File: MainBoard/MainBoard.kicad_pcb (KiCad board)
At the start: 4 copper layers, 60.5 x 128.5 mm, 46 parts, among them J2 TSW-116-12-T-S, U1 TL074CN

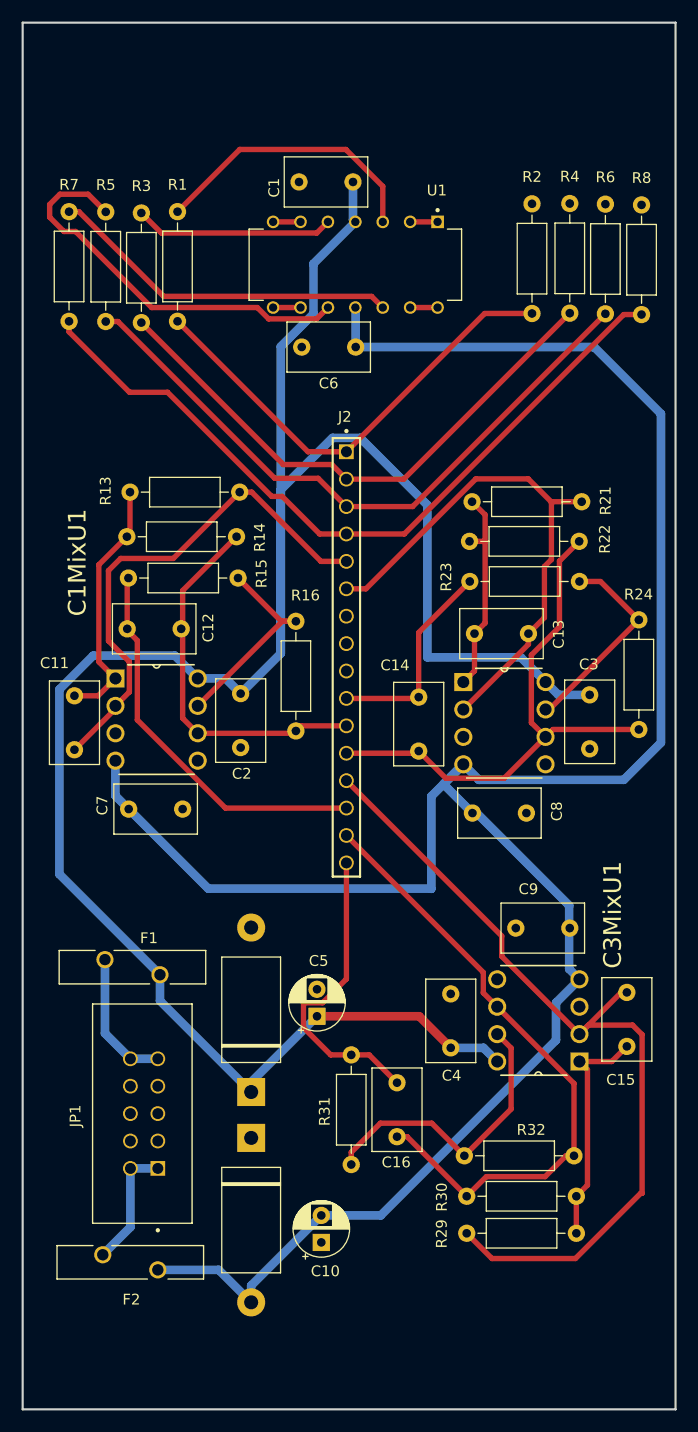
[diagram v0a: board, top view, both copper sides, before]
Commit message: added footprints and 3dmodels
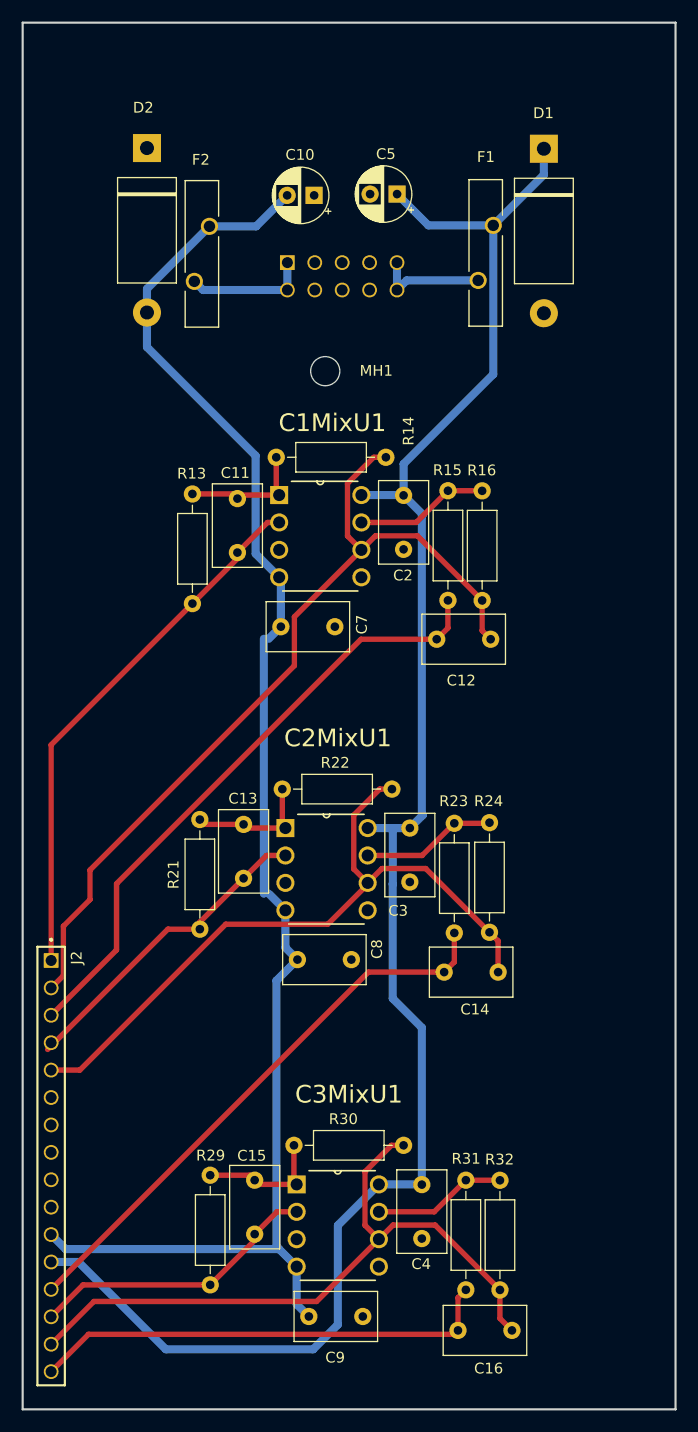
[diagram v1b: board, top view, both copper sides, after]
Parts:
- removed C1, C6: 0.1uf, Capacitor_THT:C_Disc_D7.5mm_W4.4mm_P5.00mm
- removed R1, R3, R5, R7: 1k, Resistor_THT:R_Axial_DIN0207_L6.3mm_D2.5mm_P10.16mm_Horizontal
- removed R2, R4, R6, R8: 100k, Resistor_THT:R_Axial_DIN0207_L6.3mm_D2.5mm_P10.16mm_Horizontal
- removed U1: TL074CN, TL074CN:DIP794W45P254L1969H508Q14
- added MH1: MountingHole_2.7mm_M2.5, MountingHole:MountingHole_2.7mm_M2.5, F.Cu at (129.5, 64.8)
- JP1: moved to B.Cu
- moved C10 97.0 mm to (128.5, 48.5), turned to 180 degrees
- moved F2 93.7 mm to (118.1, 53.9), turned to -90 degrees
- moved D2 92.2 mm to (113.0, 51.7)
- moved JP1 84.8 mm to (126.0, 54.7), turned to 0 degrees
- moved D1 77.1 mm to (149.8, 51.8), turned to -90 degrees
- moved C5 76.6 mm to (136.2, 48.4), turned to 180 degrees
- moved F1 73.8 mm to (144.4, 53.8), turned to -90 degrees
- moved J2 54.5 mm to (104.1, 119.4)
- moved R21 53.1 mm to (117.9, 116.5), turned to 90 degrees
- moved C9 43.4 mm to (128.0, 152.4), turned to 0 degrees
- moved C15 36.7 mm to (123.0, 139.7), turned to -90 degrees
- moved C3MixU1 28.8 mm to (134.5, 147.8), turned to 0 degrees
- moved R22 28.8 mm to (135.7, 103.5)
- moved C12 28.7 mm to (139.9, 89.6)
- moved C13 27.8 mm to (122.0, 106.8), turned to -90 degrees
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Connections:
- J2 pad 01: Input1 -> C1MixLadderOut
- J2 pad 02: Input2 -> C1MixModeOut
- J2 pad 03: Input3 -> C1MixOut
- J2 pad 04: Input4 -> C2MixLadderOut
- J2 pad 05: C1MixLadderOut -> C2MixModeOut
- J2 pad 06: C2MixLadderOut -> GND
- J2 pad 10: C2MixOut -> GND
- J2 pad 11: C1MixModeOut -> -v
- J2 pad 12: C2MixModeOut -> +v
- J2 pad 13: C3MixLadderOut -> C2MixOut
- J2 pad 14: C1MixOut -> C3MixLadderOut
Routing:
- net -v: track 216.0 -> 142.2 mm
- net Input4: track 70.2 -> 0.00 mm
- net Input3: track 60.8 -> 0.00 mm
- net Input2: track 52.1 -> 0.00 mm
- net C3MixLadderOut: track 79.1 -> 27.1 mm
- net C1MixModeOut: track 34.9 -> 81.9 mm
- net Input1: track 43.2 -> 0.00 mm
- net Net-(U1-3IN+): track 37.6 -> 0.00 mm
- net +v: track 208.0 -> 172.8 mm
- net C2MixOut: track 19.4 -> 52.6 mm
- net Net-(U1-4IN+): track 32.8 -> 0.00 mm
- net Net-(U1-1IN+): track 26.1 -> 0.00 mm
- net C1MixOut: track 36.3 -> 57.8 mm
- net C2MixLadderOut: track 49.6 -> 29.9 mm
- net Net-(U1-2IN+): track 18.5 -> 0.00 mm
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
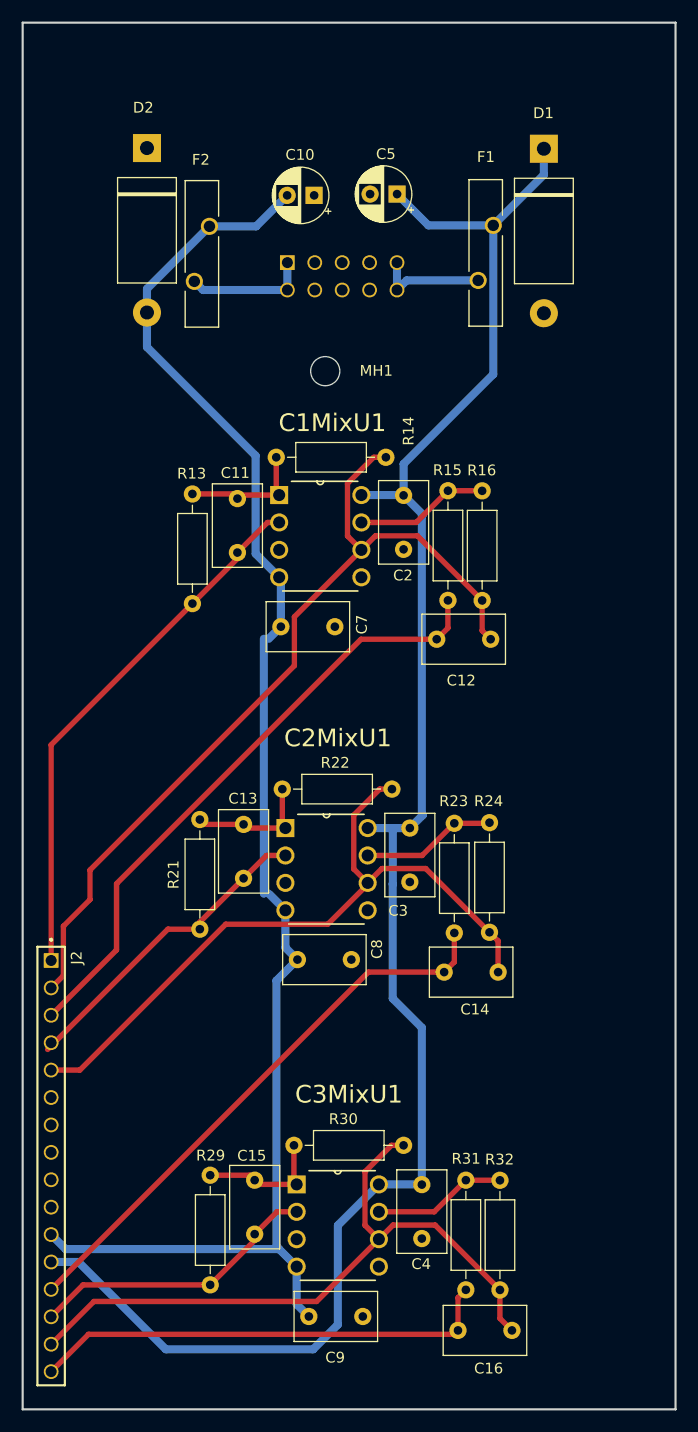
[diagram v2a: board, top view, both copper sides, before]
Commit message: replaced SPST swtiches with sub-toggle, alinged switch faceplace holes, updated 3d models
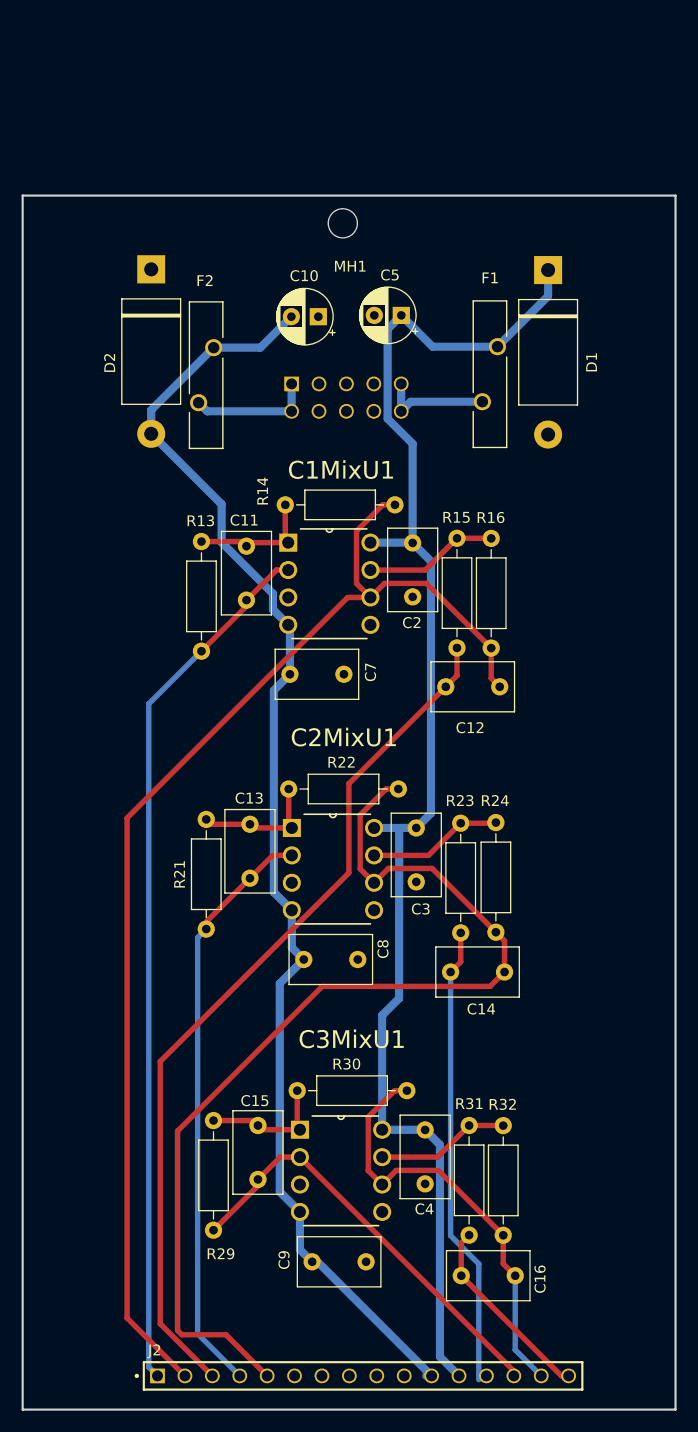
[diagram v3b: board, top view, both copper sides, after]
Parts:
- R15, R23, R31: value 220 -> 1k
- moved J2 39.7 mm to (114.0, 157.9), turned to 0 degrees
- moved MH1 13.8 mm to (131.2, 51.1)
- moved D1 11.2 mm to (150.2, 63.0)
- moved F2 11.2 mm to (118.5, 65.1)
- moved C10 11.2 mm to (128.9, 59.7)
- moved C5 11.2 mm to (136.6, 59.6)
- moved F1 11.2 mm to (144.8, 65.1)
- moved D2 11.2 mm to (113.4, 63.0)
- moved JP1 11.2 mm to (126.4, 66.0)
- moved C15 5.08 mm to (123.3, 134.7)
- moved C4 5.08 mm to (138.8, 135.1)
- moved C9 5.08 mm to (128.3, 147.3)
- moved R31 5.08 mm to (142.9, 134.7)
- moved C3MixU1 5.08 mm to (134.8, 142.7)
- moved R32 5.08 mm to (146.0, 144.8)
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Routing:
- net +v: track 172.8 -> 135.6 mm
- net C1MixModeOut: track 81.9 -> 114.3 mm
- net C1MixLadderOut: track 50.0 -> 81.0 mm
- net C2MixModeOut: track 66.3 -> 94.7 mm
- net C3MixOut: track 43.3 -> 18.4 mm
- net C2MixLadderOut: track 29.9 -> 54.5 mm
- net C3MixModeOut: track 64.2 -> 40.1 mm
- net C1MixOut: track 57.8 -> 80.8 mm
- net -v: track 142.2 -> 120.7 mm
- net C3MixLadderOut: track 27.1 -> 39.6 mm
- net C2MixOut: track 52.6 -> 42.9 mm
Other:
- board size 60.5 x 128.5 mm -> 60.5 x 112.5 mm
- board text added: "R-mods"
- board text added: "RM-MMB1-2024-v1.0.0"
